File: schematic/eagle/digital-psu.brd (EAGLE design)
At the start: 107.6 x 85.1 mm, 79 parts, among them IC1 TL072P, IC2 TLC272P, Q1 MPSA56-TO92, T3 2N3055, T4 2N3055, T5 2N3055, X1 Vout, X2 PASS_TRANSISTORS, X3 AC_IN

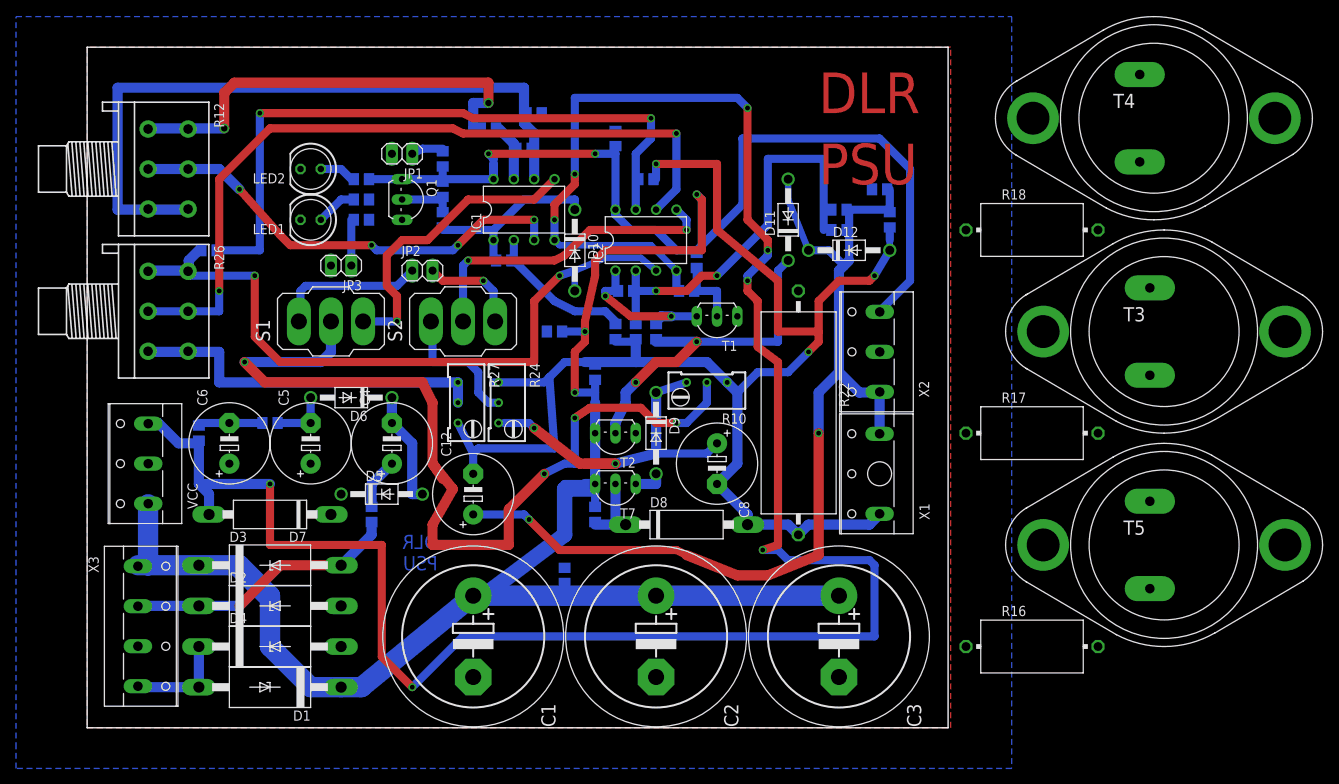
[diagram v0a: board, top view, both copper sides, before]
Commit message: removed all airwires
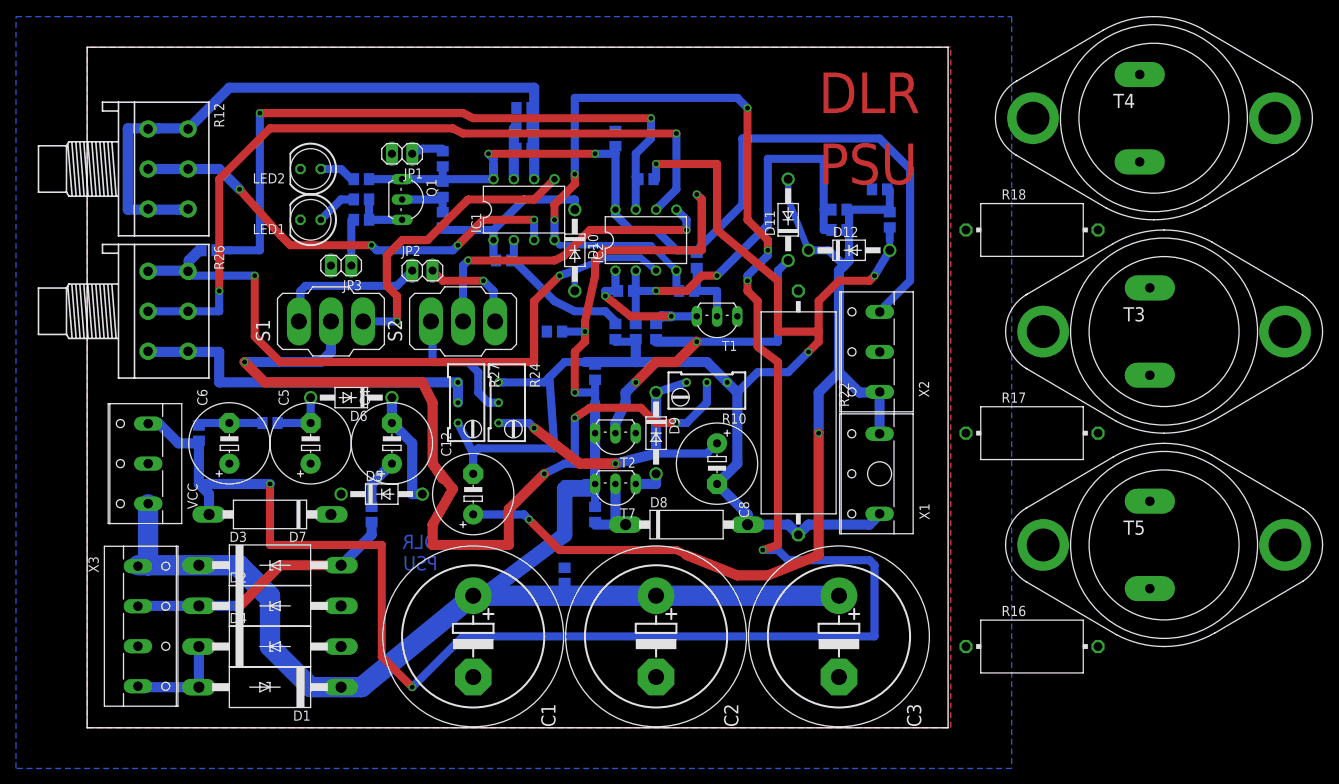
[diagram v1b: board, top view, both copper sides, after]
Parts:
- R27: value 100 -> 10k
- moved R11 4.45 mm to (52.1, 72.4), turned to 0 degrees
- moved R13 1.42 mm to (52.1, 74.9), turned to 0 degrees
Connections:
- removed net N$32: R11.1, R12.1-1, R12.2-1
- net N$20: now also R11.1, R12.1-1, R12.2-1
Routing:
- net N$32: track 55.8 -> 0.00 mm, vias 2 -> 0
- net ADJ_VOLT: track 79.8 -> 88.9 mm
- net N$20: track 86.9 -> 95.1 mm
- net N$41: track 124.4 -> 131.2 mm
- net N$11: track 0.00 -> 6.67 mm
- net N$36: track 45.1 -> 50.3 mm
- net VCC: track 362.5 -> 366.3 mm
- net N$38: track 50.4 -> 53.0 mm
- net N$23: track 7.14 -> 9.34 mm
- net VNEG: track 272.2 -> 274.1 mm
- net N$1: track 34.2 -> 35.8 mm
- net N$16: track 7.62 -> 9.21 mm
- net N$3: track 12.7 -> 14.0 mm
- net N$17: track 7.62 -> 8.89 mm
- net GND_HIGHER: track 173.1 -> 174.1 mm
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
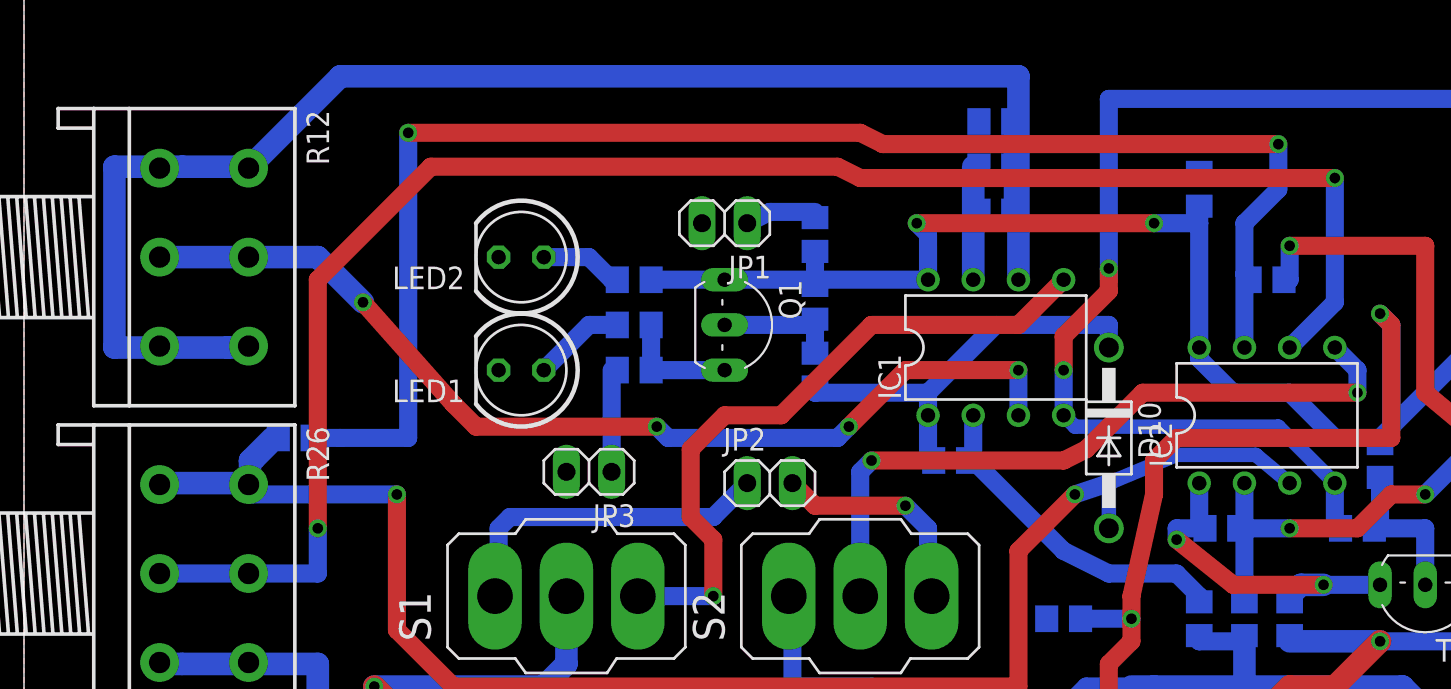
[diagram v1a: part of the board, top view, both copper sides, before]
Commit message: op amp 27k protection fixed
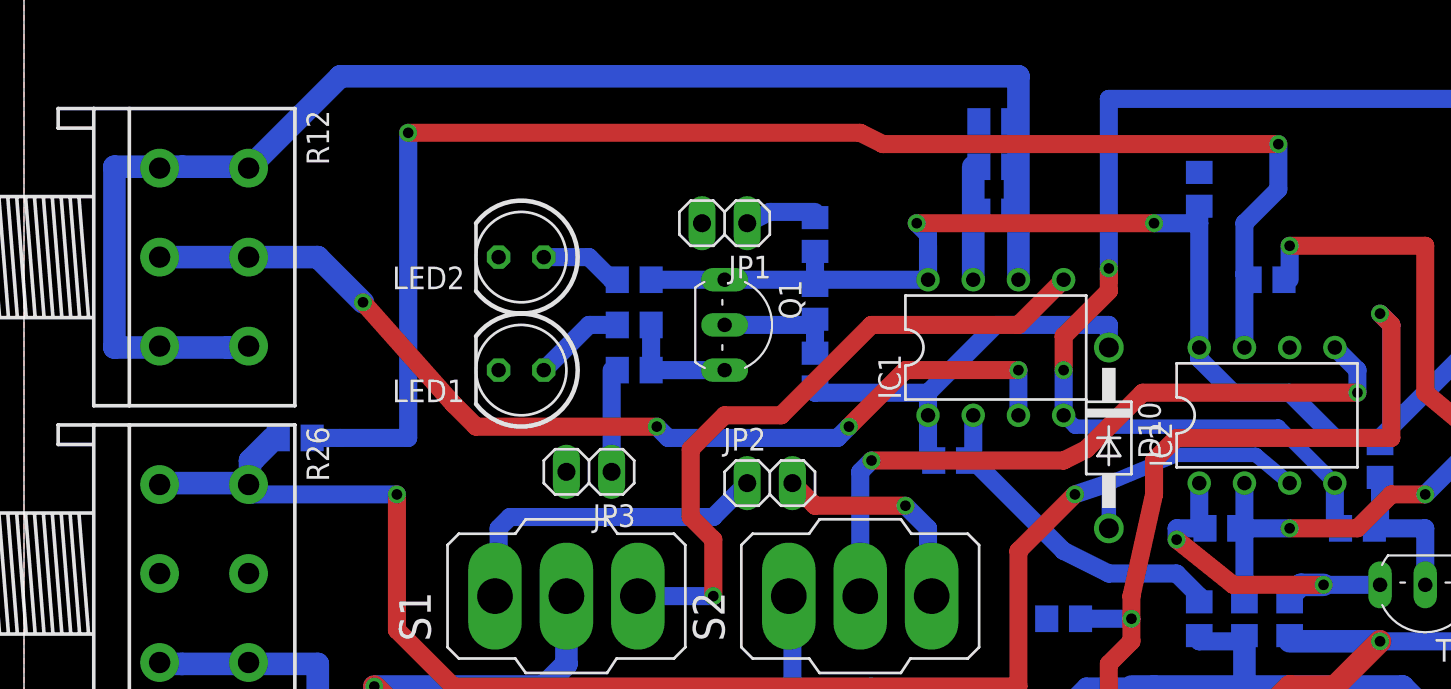
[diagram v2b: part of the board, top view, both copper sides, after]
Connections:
- new net NEG_IN_VOL_ADJ: C14.2, IC2.6, R25.1, R26.1-1, R26.2-1
- net ADJ_VOLT: now also R26.1-2, R26.2-2; no longer R25.1, R26.1-1, R26.2-1
- net GND_HIGHER: no longer C14.2
- net N$2: now also R12.1-3, R12.2-3, R13.1; no longer IC2.6, R26.1-2, R26.2-2
- net N$20: no longer R12.1-3, R12.2-3, R13.1
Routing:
- net N$2: track 95.9 -> 0.00 mm, vias 2 -> 0
- net ADJ_VOLT: track 88.9 -> 80.3 mm
- net NEG_IN_VOL_ADJ: track 0.00 -> 8.50 mm
- net N$20: track 95.1 -> 89.5 mm
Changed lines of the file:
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@@
 <contactref element="R11" pad="1"/>
 <contactref element="C13" pad="2"/>
-<contactref element="R12" pad="1-3"/>
-<contactref element="R12" pad="2-3"/>
-<contactref element="R13" pad="1"/>
 <contactref element="IC1" pad="6"/>
 <wire x1="53.34" y1="66.04" x2="53.34" y2="77.47" width="1.27" layer="16"/>
@@
 <wire x1="8.89" y1="62.23" x2="10.16" y2="62.23" width="1.27" layer="16"/>
 <wire x1="53.34" y1="77.47" x2="53.34" y2="75.25" width="1.016" layer="16"/>
-<wire x1="53.34" y1="75.25" x2="53.02" y2="74.93" width="1.016" layer="16"/>
-<wire x1="53.02" y1="74.93" x2="53.02" y2="72.39" width="1.016" layer="16"/>
 <wire x1="53.02" y1="72.39" x2="53.02" y2="69.85" width="1.016" layer="16"/>
 <wire x1="8.89" y1="62.23" x2="10" y2="62.23" width="1.016" layer="16"/>
-<wire x1="10" y1="62.23" x2="10.08" y2="62.31" width="1.016" layer="16"/>
-<wire x1="5.08" y1="62.31" x2="2.62" y2="62.31" width="1.016" layer="16"/>
 <wire x1="2.62" y1="62.31" x2="2.54" y2="62.23" width="1.016" layer="16"/>
 <wire x1="6.35" y1="72.39" x2="5.16" y2="72.39" width="1.016" layer="16"/>
 <wire x1="5.16" y1="72.39" x2="5.08" y2="72.31" width="1.016" layer="16"/>
 <wire x1="10.08" y1="72.31" x2="10.16" y2="72.39" width="1.016" layer="16"/>
+<wire x1="53.34" y1="75.25" x2="53.02" y2="72.39" width="0" layer="19" extent="16-16"/>
 </signal>
 <signal name="N$23">
@@
 <contactref element="C8" pad="-"/>
 <contactref element="D8" pad="A"/>
-<contactref element="C14" pad="2"/>
 <contactref element="R27" pad="3"/>
 <wire x1="80.01" y1="22.86" x2="85.09" y2="22.86" width="1.27" layer="16"/>
@@
 <wire x1="46.355" y1="32.385" x2="55.88" y2="32.385" width="1.016" layer="16"/>
 <wire x1="55.88" y1="32.385" x2="55.245" y2="41.275" width="1.016" layer="16"/>
-<wire x1="68.26" y1="66.04" x2="68.58" y2="66.04" width="1.016" layer="16"/>
 <wire x1="63.5" y1="46.04" x2="63.5" y2="45.72" width="1.016" layer="16"/>
 <wire x1="66.04" y1="46.04" x2="66.04" y2="45.72" width="1.016" layer="16"/>
@@
 </signal>
 <signal name="ADJ_VOLT">
-<contactref element="R25" pad="1"/>
-<contactref element="R26" pad="2-1"/>
-<contactref element="R26" pad="1-1"/>
 <contactref element="D10" pad="A"/>
 <contactref element="IC2" pad="3"/>
@@
 <wire x1="18.415" y1="53.975" x2="10.16" y2="53.975" width="1.016" layer="16"/>
 <wire x1="10.16" y1="53.975" x2="10.16" y2="54.45" width="1.016" layer="16"/>
-<wire x1="10.16" y1="54.45" x2="10.08" y2="54.53" width="1.016" layer="16"/>
-<wire x1="10.08" y1="54.53" x2="5.08" y2="54.53" width="1.016" layer="16"/>
-<wire x1="10.08" y1="54.53" x2="10.08" y2="55.8" width="1.016" layer="16"/>
-<wire x1="10.08" y1="55.8" x2="10.16" y2="55.88" width="1.016" layer="16"/>
-<wire x1="10.16" y1="55.88" x2="10.48" y2="55.88" width="1.016" layer="16"/>
-<wire x1="10.48" y1="55.88" x2="11.75" y2="57.15" width="1.016" layer="16"/>
-</signal>
-<signal name="N$2">
+<contactref element="R26" pad="2-2"/>
 <contactref element="R26" pad="1-2"/>
-<contactref element="R26" pad="2-2"/>
-<contactref element="IC2" pad="6"/>
-<wire x1="71.12" y1="71.755" x2="44.45" y2="71.755" width="1.016" layer="1"/>
-<wire x1="44.45" y1="71.755" x2="43.18" y2="72.39" width="1.016" layer="1"/>
-<wire x1="43.18" y1="72.39" x2="20.32" y2="72.39" width="1.016" layer="1"/>
-<wire x1="20.32" y1="72.39" x2="13.97" y2="66.04" width="1.016" layer="1"/>
-<wire x1="13.97" y1="66.04" x2="13.97" y2="52.07" width="1.016" layer="1"/>
-<via x="13.97" y="52.07" extent="1-16" drill="0.6" shape="square"/>
-<wire x1="5.08" y1="49.53" x2="10.08" y2="49.53" width="1.016" layer="16"/>
-<wire x1="13.97" y1="49.53" x2="13.97" y2="52.07" width="1.016" layer="16"/>
-<wire x1="68.58" y1="62.23" x2="71.12" y2="64.77" width="1.016" layer="16"/>
-<wire x1="71.12" y1="64.77" x2="71.12" y2="71.755" width="1.016" layer="16"/>
-<via x="71.12" y="71.755" extent="1-16" drill="0.6" shape="square"/>
-<wire x1="10.08" y1="49.53" x2="13.97" y2="49.53" width="1.016" layer="16"/>
+<wire x1="10.08" y1="49.53" x2="10.16" y2="53.975" width="0" layer="19" extent="16-16"/>
+<wire x1="5.08" y1="49.53" x2="10.08" y2="49.53" width="0" layer="19" extent="1-1"/>
 </signal>
 <signal name="N$4">
@@
 </polygon>
 </signal>
+<signal name="NEG_IN_VOL_ADJ">
+<contactref element="R25" pad="1"/>
+<contactref element="R26" pad="2-1"/>
+<contactref element="R26" pad="1-1"/>
+<contactref element="IC2" pad="6"/>
+<contactref element="C14" pad="2"/>
+<wire x1="10.08" y1="54.53" x2="5.08" y2="54.53" width="1.016" layer="16"/>
+<wire x1="10.08" y1="54.53" x2="10.08" y2="55.8" width="1.016" layer="16"/>
+<wire x1="10.08" y1="55.8" x2="10.16" y2="55.88" width="1.016" layer="16"/>
+<wire x1="10.16" y1="55.88" x2="10.48" y2="55.88" width="1.016" layer="16"/>
+<wire x1="10.48" y1="55.88" x2="11.75" y2="57.15" width="1.016" layer="16"/>
+<wire x1="68.58" y1="62.23" x2="68.26" y2="66.04" width="0" layer="19" extent="16-16"/>
+<wire x1="11.75" y1="57.15" x2="68.58" y2="62.23" width="0" layer="19" extent="16-16"/>
+</signal>
+<signal name="N$2">
+<contactref element="R12" pad="1-3"/>
+<contactref element="R12" pad="2-3"/>
+<contactref element="R13" pad="1"/>
+<wire x1="10.08" y1="62.31" x2="53.02" y2="74.93" width="0" layer="19" extent="16-16"/>
+<wire x1="5.08" y1="62.31" x2="10.08" y2="62.31" width="0" layer="19" extent="1-1"/>
+</signal>
 </signals>

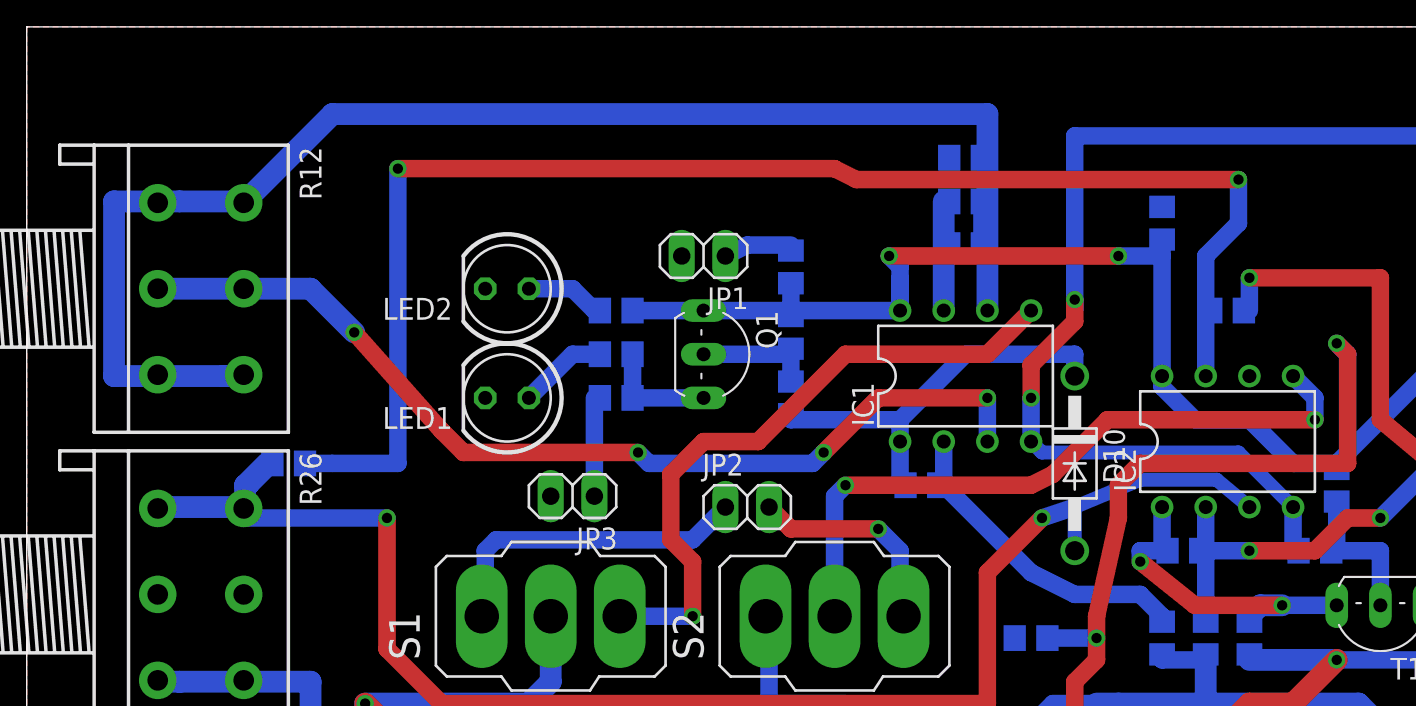
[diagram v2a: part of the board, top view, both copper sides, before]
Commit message: added .spice files. In process of joining the two separate grounds
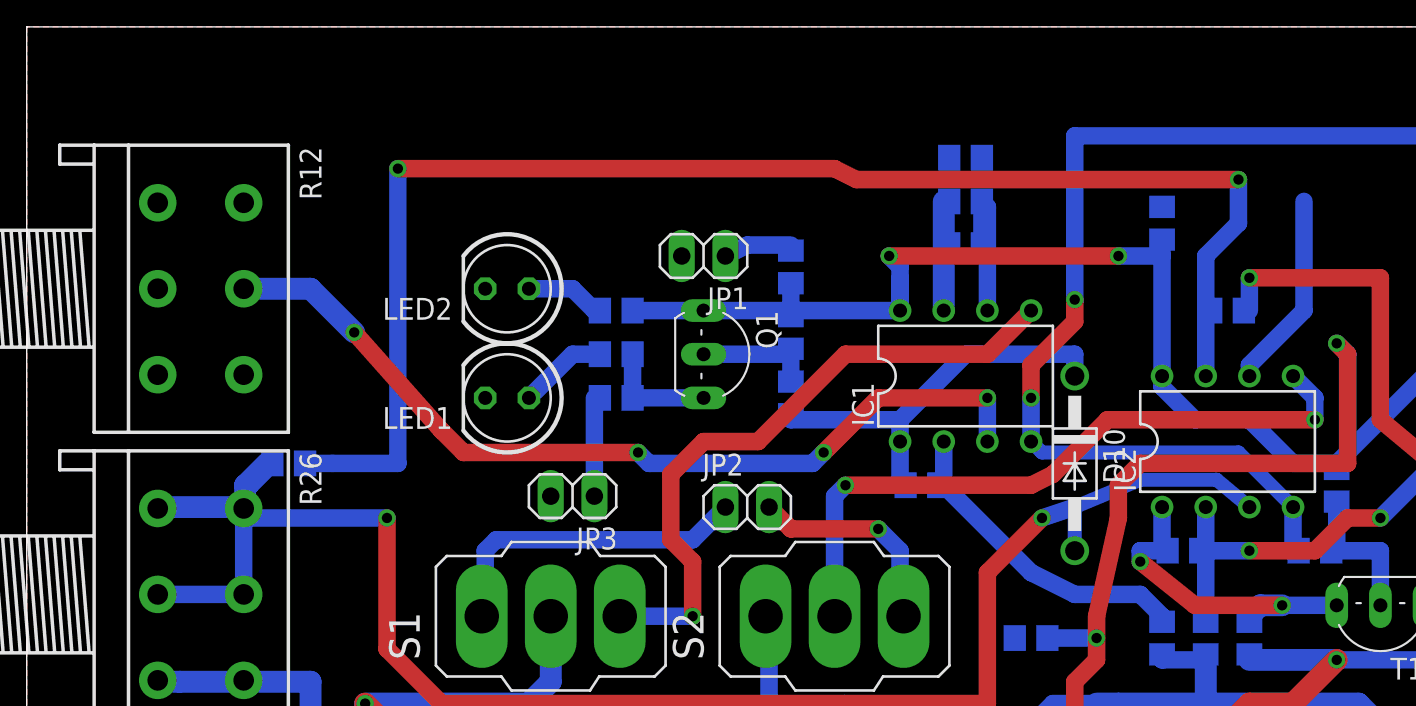
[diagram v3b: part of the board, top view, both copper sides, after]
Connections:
- removed net N$2: R12.1-3, R12.2-3, R13.1
- new net N$32: R12.1-1, R12.2-1, R13.1
- net N$20: now also R12.1-3, R12.2-3; no longer R12.1-1, R12.2-1
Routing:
- net N$20: track 89.5 -> 9.02 mm
- net NEG_IN_VOL_ADJ: track 8.50 -> 20.0 mm
- net ADJ_VOLT: track 80.3 -> 89.8 mm
- net ADJ_CURR: track 56.8 -> 51.8 mm
